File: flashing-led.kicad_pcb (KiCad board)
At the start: 2 copper layers, 6 parts, among them U1 NE555

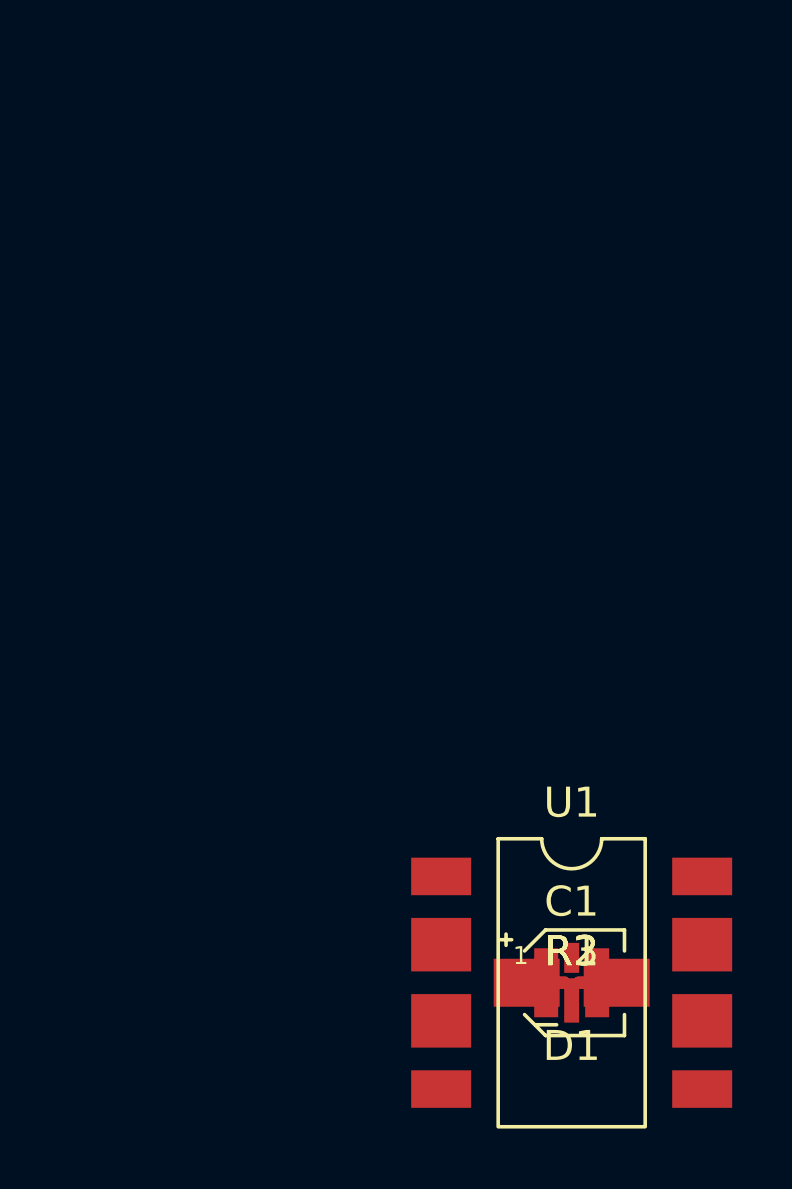
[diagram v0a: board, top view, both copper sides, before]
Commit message: PCB layout and traces
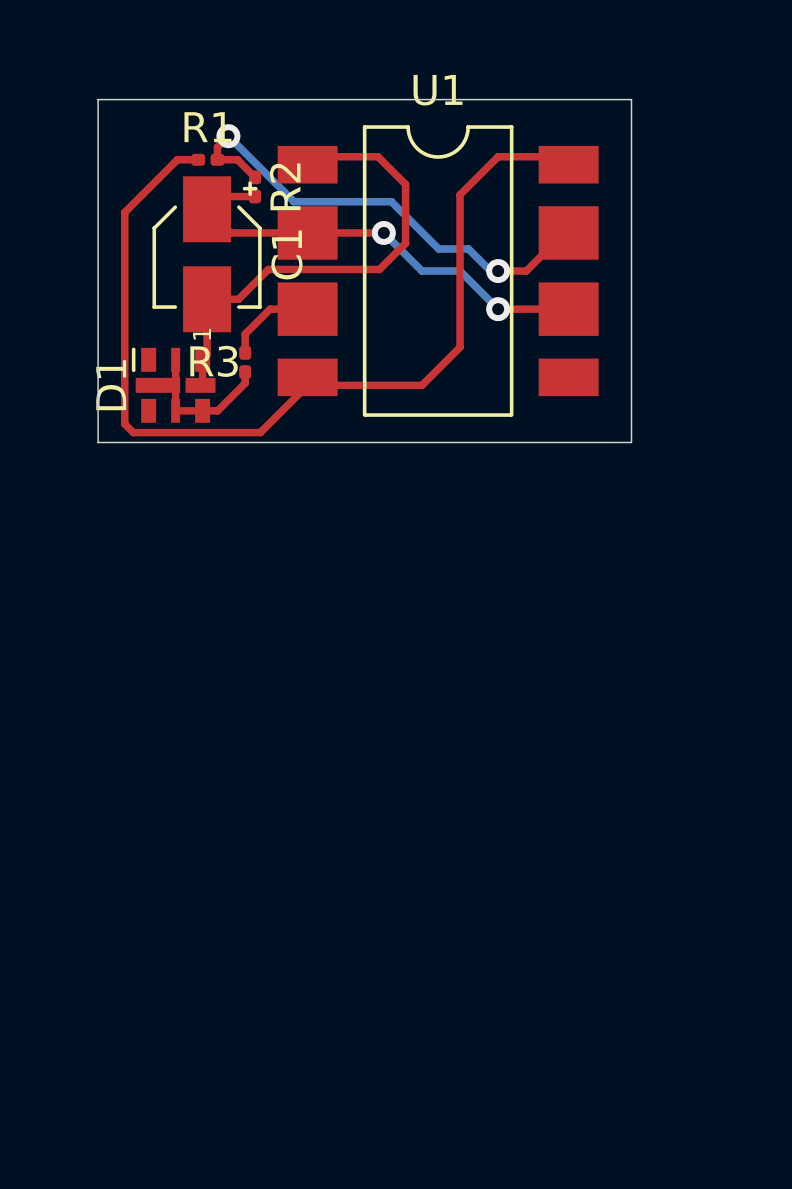
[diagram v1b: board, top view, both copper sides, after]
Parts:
- moved R1 30.0 mm to (136.4, 77.6)
- moved R2 28.6 mm to (137.9, 78.5), turned to 270 degrees
- moved C1 27.2 mm to (136.3, 80.7), turned to 270 degrees
- moved U1 24.1 mm to (144.1, 81.3)
- moved D1 23.9 mm to (135.3, 85.1), turned to 270 degrees
- moved R3 23.4 mm to (137.6, 84.3), turned to 90 degrees
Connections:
- D1 pad 5: (no net) -> Net-(D1-Pad2)
- D1 pad 6: (no net) -> Net-(D1-Pad2)
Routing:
- net +9V: track 0.00 -> 31.9 mm
- net dis: track 0.00 -> 16.2 mm, vias 0 -> 2
- net GND: track 0.00 -> 16.0 mm
- net tr_thr: track 0.00 -> 15.2 mm, vias 0 -> 2
- net Net-(D1-Pad2): track 0.00 -> 5.83 mm
- net Net-(R3-Pad2): track 0.00 -> 3.05 mm
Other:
- board outline added: 17.8 x 11.4 mm

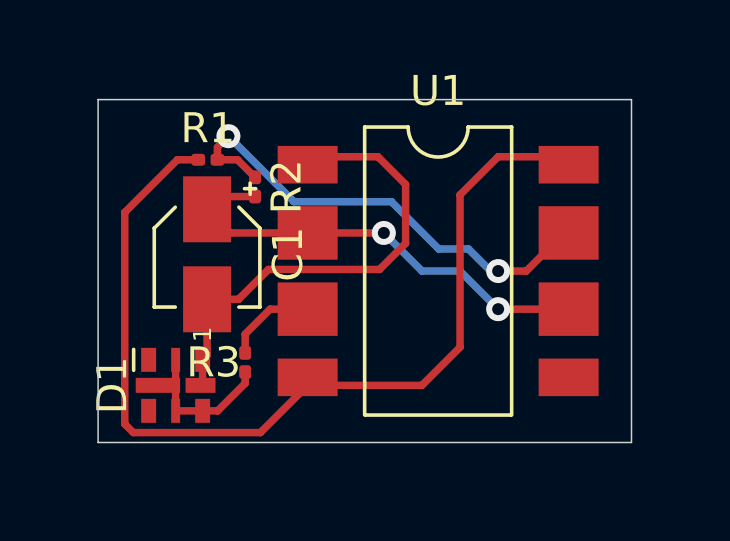
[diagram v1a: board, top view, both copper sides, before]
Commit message: added Vcc and GND pours
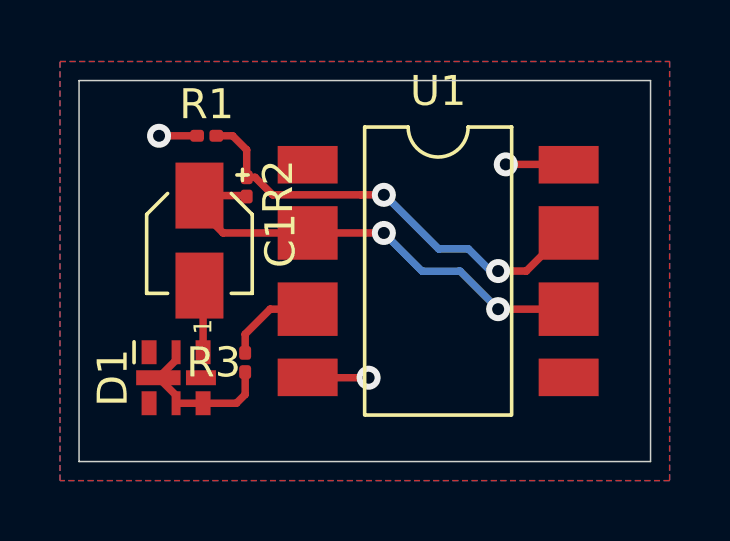
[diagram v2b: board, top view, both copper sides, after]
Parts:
- moved R1 0.80 mm to (136.3, 76.8)
- moved C1 0.52 mm to (136.1, 80.3)
- moved R2 0.28 mm to (137.7, 78.5)
- moved D1 0.25 mm to (135.3, 84.8)
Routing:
- net +9V: track 31.9 -> 5.61 mm, vias 0 -> 3
- net GND: track 16.0 -> 2.49 mm
- net dis: track 16.2 -> 14.3 mm
- added copper zone on B.Cu, net +9V
- added copper zone on F.Cu, net GND
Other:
- board size 17.8 x 11.4 mm -> 19 x 12.7 mm
